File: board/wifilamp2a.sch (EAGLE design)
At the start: 6 parts

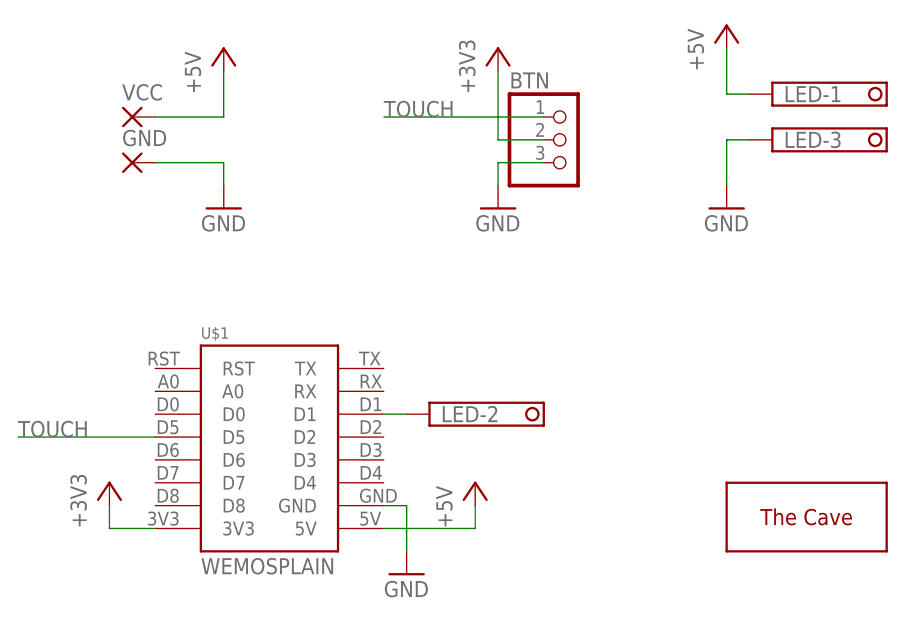
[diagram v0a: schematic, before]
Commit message: [board] Update board to rev 2.1
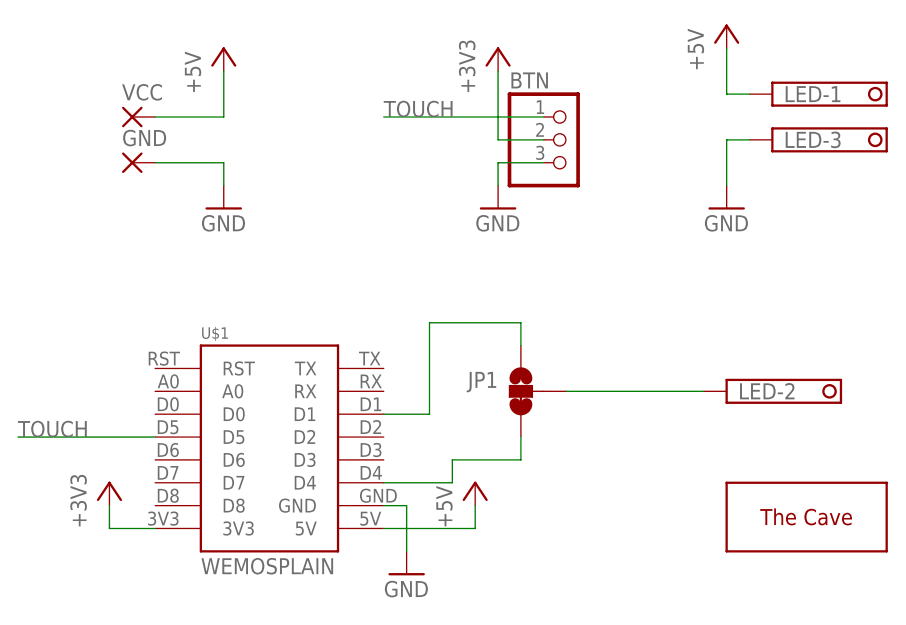
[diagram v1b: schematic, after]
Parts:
- added JP1: JUMPER-SMT_3_1-NC_TRACE_NO-SILK, SparkFun-Jumpers:JUMPER-SMT_3_1-NC_TRACE_NO-SILK
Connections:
- new net N$1: JP1.1, U$1.D1
- new net N$3: JP1.2, LED-2.K
- net N$2: now also JP1.3, U$1.D4; no longer LED-2.K, U$1.D1
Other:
- moved on the sheet: LED-2
